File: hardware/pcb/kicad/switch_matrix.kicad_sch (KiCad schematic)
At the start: 38 parts, among them SW1 SW_socket, SW10 SW_socket, SW11 SW_socket, SW12 SW_socket, SW13 SW_socket, SW14 SW_socket, SW15 SW_socket, SW16 SW_socket, SW2 SW_socket, SW3 SW_socket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

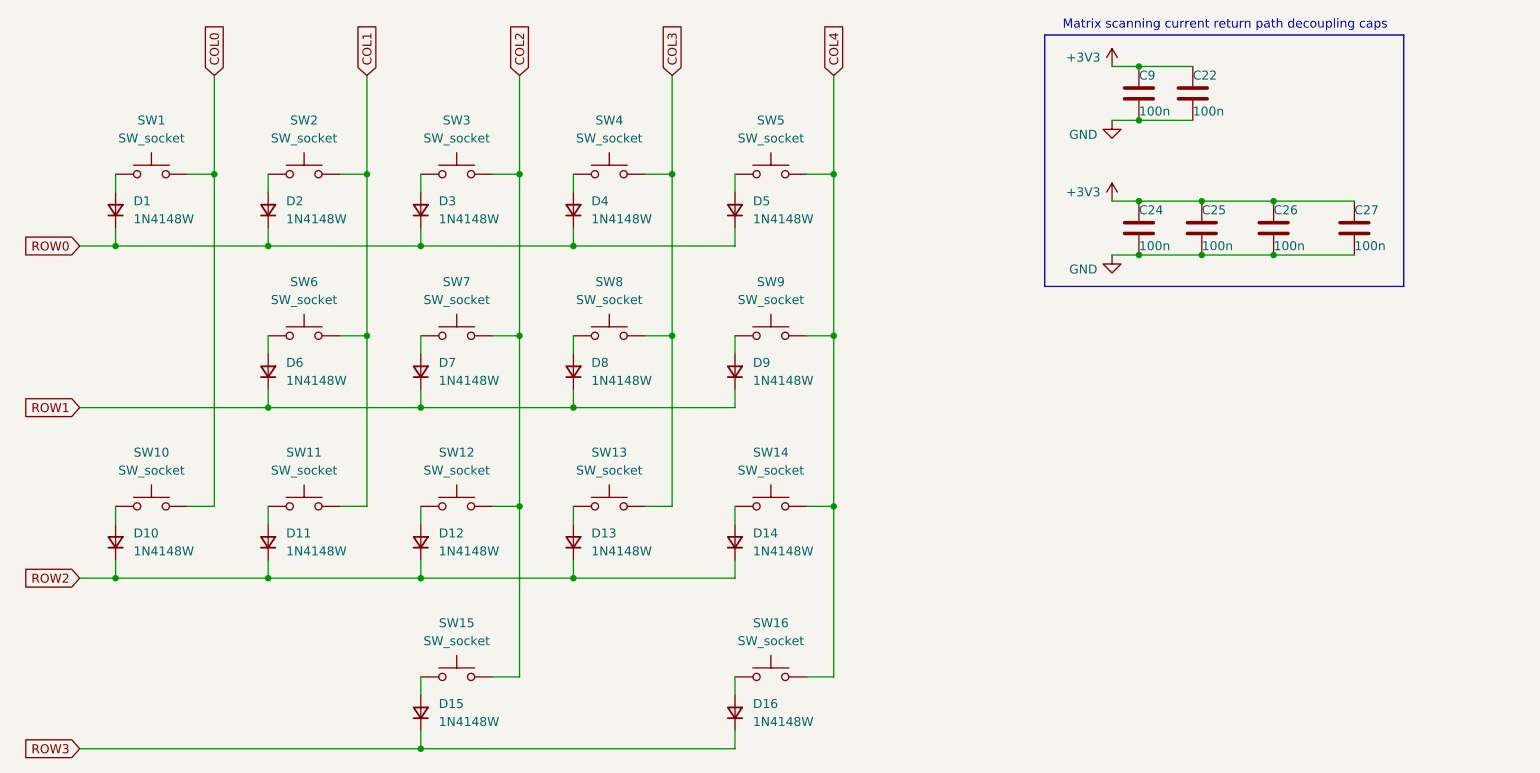
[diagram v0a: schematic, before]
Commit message: Reformatting, removing old files, add better documentation about licenses
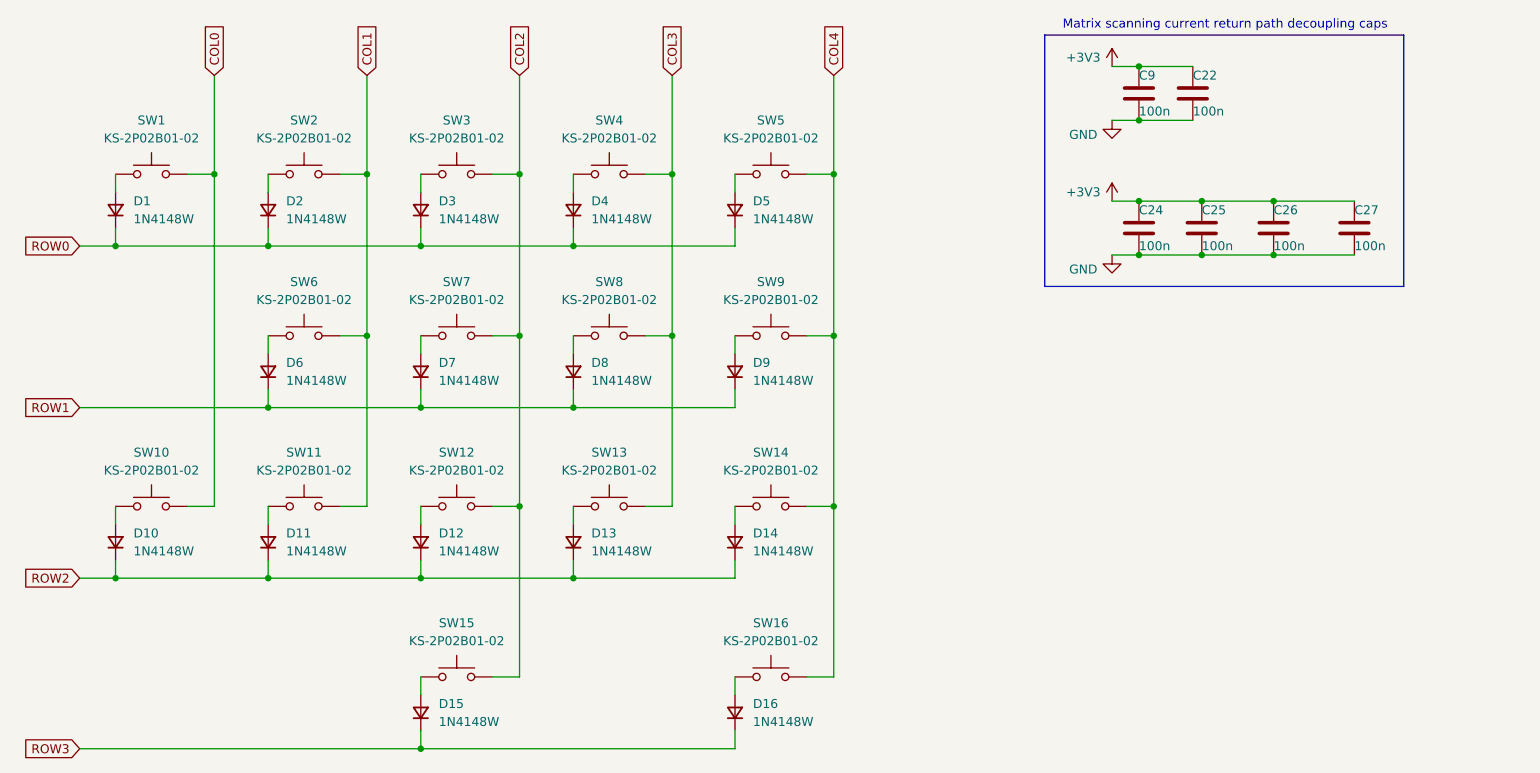
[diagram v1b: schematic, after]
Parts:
- SW1, SW10, SW11, SW12, SW13, SW14, SW15, SW16, SW2, SW3, SW4, SW5, SW6, SW7, SW8, SW9: value SW_socket -> KS-2P02B01-02; LCSC (none) -> C9900051050
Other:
- title: Mathpad -> Mathpad PCB
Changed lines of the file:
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@@
 	(paper "A4")
 	(title_block
-		(title "Mathpad")
-		(date "2025-04-05")
+		(title "Mathpad PCB")
+		(date "2025-04-07")
 		(rev "1.6")
 		(company "Summacogni OÜ")
@@
 			)
 		)
-		(property "Value" "SW_socket"
+		(property "Value" "KS-2P02B01-02"
 			(at 107.95 104.14 0)
 			(effects
@@
 			)
 		)
+		(property "LCSC" "C9900051050"
+			(at 107.95 109.22 0)
+			(effects
+				(font
+					(size 1.27 1.27)
+				)
+				(hide yes)
+			)
+		)
 		(pin "1"
 		)
@@
 			)
 		)
-		(property "Value" "SW_socket"
+		(property "Value" "KS-2P02B01-02"
 			(at 107.95 57.15 0)
 			(effects
@@
 			)
 		)
+		(property "LCSC" "C9900051050"
+			(at 107.95 62.23 0)
+			(effects
+				(font
+					(size 1.27 1.27)
+				)
+				(hide yes)
+			)
+		)
 		(pin "1"
 		)
@@
 			)
 		)
-		(property "Value" "SW_socket"
+		(property "Value" "KS-2P02B01-02"
 			(at 151.13 104.14 0)
 			(effects
@@
 			)
 		)
+		(property "LCSC" "C9900051050"
+			(at 151.13 109.22 0)
+			(effects
+				(font
+					(size 1.27 1.27)
+				)
+				(hide yes)
+			)
+		)
 		(pin "1"
 		)
@@
 			)
 		)
-		(property "Value" "SW_socket"
+		(property "Value" "KS-2P02B01-02"
 			(at 173.99 104.14 0)
 			(effects
@@
 			)
 		)
+		(property "LCSC" "C9900051050"
+			(at 173.99 109.22 0)
+			(effects
+				(font
+					(size 1.27 1.27)
+				)
+				(hide yes)
+			)
+		)
 		(pin "1"
 		)
@@
 			)
 		)
-		(property "Value" "SW_socket"
+		(property "Value" "KS-2P02B01-02"
 			(at 151.13 80.01 0)
 			(effects
@@
 			)
 		)
+		(property "LCSC" "C9900051050"
+			(at 151.13 85.09 0)
+			(effects
+				(font
+					(size 1.27 1.27)
+				)
+				(hide yes)
+			)
+		)
 		(pin "1"
 		)
@@
 			)
 		)
-		(property "Value" "SW_socket"
+		(property "Value" "KS-2P02B01-02"
 			(at 86.36 104.14 0)
 			(effects
@@
 			)
 		)
+		(property "LCSC" "C9900051050"
+			(at 86.36 109.22 0)
+			(effects
+				(font
+					(size 1.27 1.27)
+				)
+				(hide yes)
+			)
+		)
 		(pin "1"
 		)
@@
 			)
 		)
-		(property "Value" "SW_socket"
+		(property "Value" "KS-2P02B01-02"
 			(at 86.36 57.15 0)
 			(effects
@@
 			)
 		)
+		(property "LCSC" "C9900051050"
+			(at 86.36 62.23 0)
+			(effects
+				(font
+					(size 1.27 1.27)
+				)
+				(hide yes)
+			)
+		)
 		(pin "1"
 		)
@@
 			)
 		)
-		(property "Value" "SW_socket"
+		(property "Value" "KS-2P02B01-02"
 			(at 173.99 128.27 0)
 			(effects
@@
 			)
 		)
+		(property "LCSC" "C9900051050"
+			(at 173.99 133.35 0)
+			(effects
+				(font
+					(size 1.27 1.27)
+				)
+				(hide yes)
+			)
+		)
 		(pin "1"
 		)
@@
 			)
 		)
-		(property "Value" "SW_socket"
+		(property "Value" "KS-2P02B01-02"
 			(at 107.95 80.01 0)
 			(effects
@@
 			)
 		)
+		(property "LCSC" "C9900051050"
+			(at 107.95 85.09 0)
+			(effects
+				(font
+					(size 1.27 1.27)
+				)
+				(hide yes)
+			)
+		)
 		(pin "1"
 		)
@@
 			)
 		)
-		(property "Value" "SW_socket"
+		(property "Value" "KS-2P02B01-02"
 			(at 129.54 80.01 0)
 			(effects
@@
 			)
 		)
+		(property "LCSC" "C9900051050"
+			(at 129.54 85.09 0)
+			(effects
+				(font
+					(size 1.27 1.27)
+				)
+				(hide yes)
+			)
+		)
 		(pin "1"
 		)
@@
 			)
 		)
-		(property "Value" "SW_socket"
+		(property "Value" "KS-2P02B01-02"
 			(at 129.54 104.14 0)
 			(effects
@@
 			)
 		)
+		(property "LCSC" "C9900051050"
+			(at 129.54 109.22 0)
+			(effects
+				(font
+					(size 1.27 1.27)
+				)
+				(hide yes)
+			)
+		)
 		(pin "1"
 		)
@@
 			)
 		)
-		(property "Value" "SW_socket"
+		(property "Value" "KS-2P02B01-02"
 			(at 129.54 128.27 0)
 			(effects
@@
 			)
 		)
+		(property "LCSC" "C9900051050"
+			(at 129.54 133.35 0)
+			(effects
+				(font
+					(size 1.27 1.27)
+				)
+				(hide yes)
+			)
+		)
 		(pin "1"
 		)
@@
 			)
 		)
-		(property "Value" "SW_socket"
+		(property "Value" "KS-2P02B01-02"
 			(at 129.54 57.15 0)
 			(effects
@@
 			)
 		)
+		(property "LCSC" "C9900051050"
+			(at 129.54 62.23 0)
+			(effects
+				(font
+					(size 1.27 1.27)
+				)
+				(hide yes)
+			)
+		)
 		(pin "1"
 		)
@@
 			)
 		)
-		(property "Value" "SW_socket"
+		(property "Value" "KS-2P02B01-02"
 			(at 151.13 57.15 0)
 			(effects
@@
 			)
 		)
+		(property "LCSC" "C9900051050"
+			(at 151.13 62.23 0)
+			(effects
+				(font
+					(size 1.27 1.27)
+				)
+				(hide yes)
+			)
+		)
 		(pin "1"
 		)
@@
 			)
 		)
-		(property "Value" "SW_socket"
+		(property "Value" "KS-2P02B01-02"
 			(at 173.99 57.15 0)
 			(effects
@@
 			)
 		)
+		(property "LCSC" "C9900051050"
+			(at 173.99 62.23 0)
+			(effects
+				(font
+					(size 1.27 1.27)
+				)
+				(hide yes)
+			)
+		)
 		(pin "1"
 		)
@@
 			)
 		)
-		(property "Value" "SW_socket"
+		(property "Value" "KS-2P02B01-02"
 			(at 173.99 80.01 0)
 			(effects
@@
 			(at 173.99 85.09 0)
 			(effects
+				(font
+					(size 1.27 1.27)
+				)
+				(hide yes)
+			)
+		)
+		(property "LCSC" "C9900051050"
+			(at 173.99 85.09 0)
+			(effects

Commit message: Minor modifications to the pcb
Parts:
- SW1, SW10, SW11, SW12, SW13, SW14, SW15, SW16, SW2, SW3, SW4, SW5, SW6, SW7, SW8, SW9: JLCPCB Part # (none) -> C18212911; LCSC C9900051050 -> (none)

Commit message: Put hotswap socket on the correct layer
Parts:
- SW4: now in the parts list
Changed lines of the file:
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@@
 		(unit 1)
 		(exclude_from_sim no)
-		(in_bom no)
+		(in_bom yes)
 		(on_board yes)
 		(dnp no)

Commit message: Add MPN and purchase links to all components
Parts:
- C22, C24, C25, C26, C27, C9: value 100n -> 100nF X7R ±10% 16V; MPN  100nF 10% 10V 0402 -> CL05B104KO5NNNC; Purchase link (none) -> https://lcsc.com/product-detail/Multilayer-Ceramic-Capacito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
- D1, D10, D11, D12, D13, D14, D15, D16, D2, D3, D4, D5, D6, D7, D8, D9: value 1N4148W -> 75V 4ns 150mA; MPN  (none) -> 1N4148W; Purchase link (none) -> https://lcsc.com/product-detail/Switching-Diodes_ST-Semtech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
- SW1, SW10, SW11, SW12, SW13, SW14, SW15, SW16, SW2, SW3, SW4, SW5, SW6, SW7, SW8, SW9: MPN  (none) -> KS-2P02B01-02; Purchase link (none) -> https://www.alibaba.com/product-detail/GATERON-Customized-D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
